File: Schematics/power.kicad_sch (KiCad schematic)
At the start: 3 parts, among them U5 AMS1117-3.3

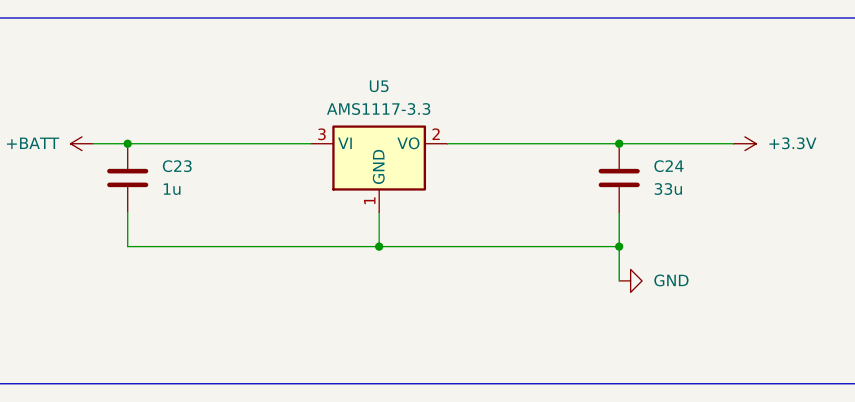
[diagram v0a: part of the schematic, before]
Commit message: added LCSC numbers and footprint values, need to connect schemeatic pins, then can start layout
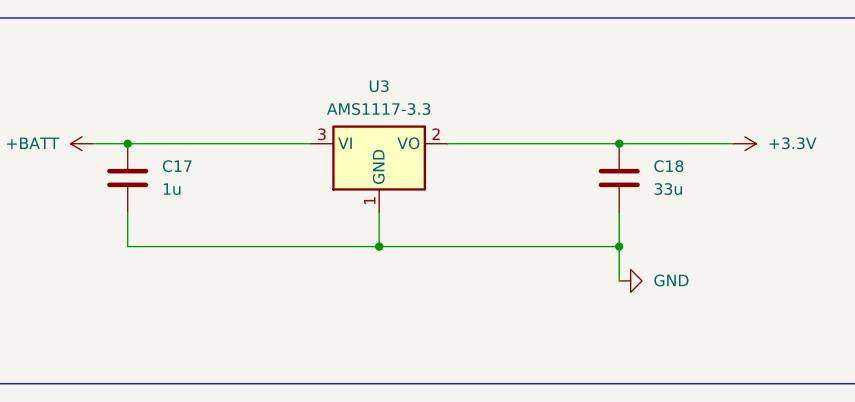
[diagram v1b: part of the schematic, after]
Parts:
- C17: renamed from C23; LCSC Part (none) -> C28323
- C18: renamed from C24; LCSC Part (none) -> C432920
- U3: renamed from U5; LCSC Part (none) -> C6186
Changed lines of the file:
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@@
 		(dnp no)
 		(fields_autoplaced yes)
-		(property "Reference" "#PWR066"
+		(property "Reference" "#PWR042"
 			(at 101.6 30.48 0)
 			(effects
@@
 			(project "flightcomputer2"
 				(path "/6cb3dda3-5fe8-4715-b831-354360aa3199/ba4deb13-717a-43bb-a60d-abfd8de92de6"
-					(reference "#PWR066")
+					(reference "#PWR042")
 					(unit 1)
 				)
@@
 		(on_board yes)
 		(dnp no)
-		(property "Reference" "C24"
+		(property "Reference" "C18"
 			(at 96.52 33.0199 0)
 			(effects
@@
 			)
 		)
+		(property "Sim.Device" ""
+			(at 92.71 34.29 0)
+			(effects
+				(font
+					(size 1.27 1.27)
+				)
+				(hide yes)
+			)
+		)
+		(property "Sim.Type" ""
+			(at 92.71 34.29 0)
+			(effects
+				(font
+					(size 1.27 1.27)
+				)
+				(hide yes)
+			)
+		)
+		(property "LCSC Part" "C432920"
+			(at 92.71 34.29 0)
+			(effects
+				(font
+					(size 1.27 1.27)
+				)
+				(hide yes)
+			)
+		)
 		(pin "2"
 		)
@@
 			(project "flightcomputer2"
 				(path "/6cb3dda3-5fe8-4715-b831-354360aa3199/ba4deb13-717a-43bb-a60d-abfd8de92de6"
-					(reference "C24")
+					(reference "C18")
 					(unit 1)
 				)
@@
 		(dnp no)
 		(fields_autoplaced yes)
-		(property "Reference" "#PWR05"
+		(property "Reference" "#PWR040"
 			(at 38.1 30.48 0)
 			(effects
@@
 			(project ""
 				(path "/6cb3dda3-5fe8-4715-b831-354360aa3199/ba4deb13-717a-43bb-a60d-abfd8de92de6"
-					(reference "#PWR05")
+					(reference "#PWR040")
 					(unit 1)
 				)
@@
 		(dnp no)
 		(fields_autoplaced yes)
-		(property "Reference" "U5"
+		(property "Reference" "U3"
 			(at 66.04 24.13 0)
 			(effects
@@
 			)
 		)
+		(property "Sim.Device" ""
+			(at 66.04 30.48 0)
+			(effects
+				(font
+					(size 1.27 1.27)
+				)
+				(hide yes)
+			)
+		)
+		(property "Sim.Type" ""
+			(at 66.04 30.48 0)
+			(effects
+				(font
+					(size 1.27 1.27)
+				)
+				(hide yes)
+			)
+		)
+		(property "LCSC Part" "C6186"
+			(at 66.04 30.48 0)
+			(effects
+				(font
+					(size 1.27 1.27)
+				)
+				(hide yes)
+			)
+		)
 		(pin "2"
 		)
@@
 			(project "flightcomputer2"
 				(path "/6cb3dda3-5fe8-4715-b831-354360aa3199/ba4deb13-717a-43bb-a60d-abfd8de92de6"
-					(reference "U5")
+					(reference "U3")
 					(unit 1)
 				)
@@
 		(dnp no)
 		(fields_autoplaced yes)
-		(property "Reference" "#PWR058"
+		(property "Reference" "#PWR041"
 			(at 99.06 45.72 0)
 			(effects
@@
 			(project "flightcomputer2"
 				(path "/6cb3dda3-5fe8-4715-b831-354360aa3199/ba4deb13-717a-43bb-a60d-abfd8de92de6"
-					(reference "#PWR058")
+					(reference "#PWR041")
 					(unit 1)
 				)
@@
 		(dnp no)
 		(fields_autoplaced yes)
-		(property "Reference" "C23"
+		(property "Reference" "C17"
 			(at 41.91 33.0199 0)
 			(effects
@@
 			)
 		)
+		(property "Sim.Device" ""
+			(at 38.1 34.29 0)
+			(effects
+				(font
+					(size 1.27 1.27)
+				)
+				(hide yes)
+			)
+		)
+		(property "Sim.Type" ""
+			(at 38.1 34.29 0)
+			(effects
+				(font
+					(size 1.27 1.27)
+				)
+				(hide yes)
+			)
+		)
+		(property "LCSC Part" "C28323"
+			(at 38.1 34.29 0)
+			(effects
+				(font
+					(size 1.27 1.27)
+				)
+				(hide yes)
+			)
+		)
 		(pin "1"
 		)
@@
 			(project "flightcomputer2"
 				(path "/6cb3dda3-5fe8-4715-b831-354360aa3199/ba4deb13-717a-43bb-a60d-abfd8de92de6"
-					(reference "C23")
-					(unit 1)
-				)
+					(reference "C17")
+					(unit 1)
+				)

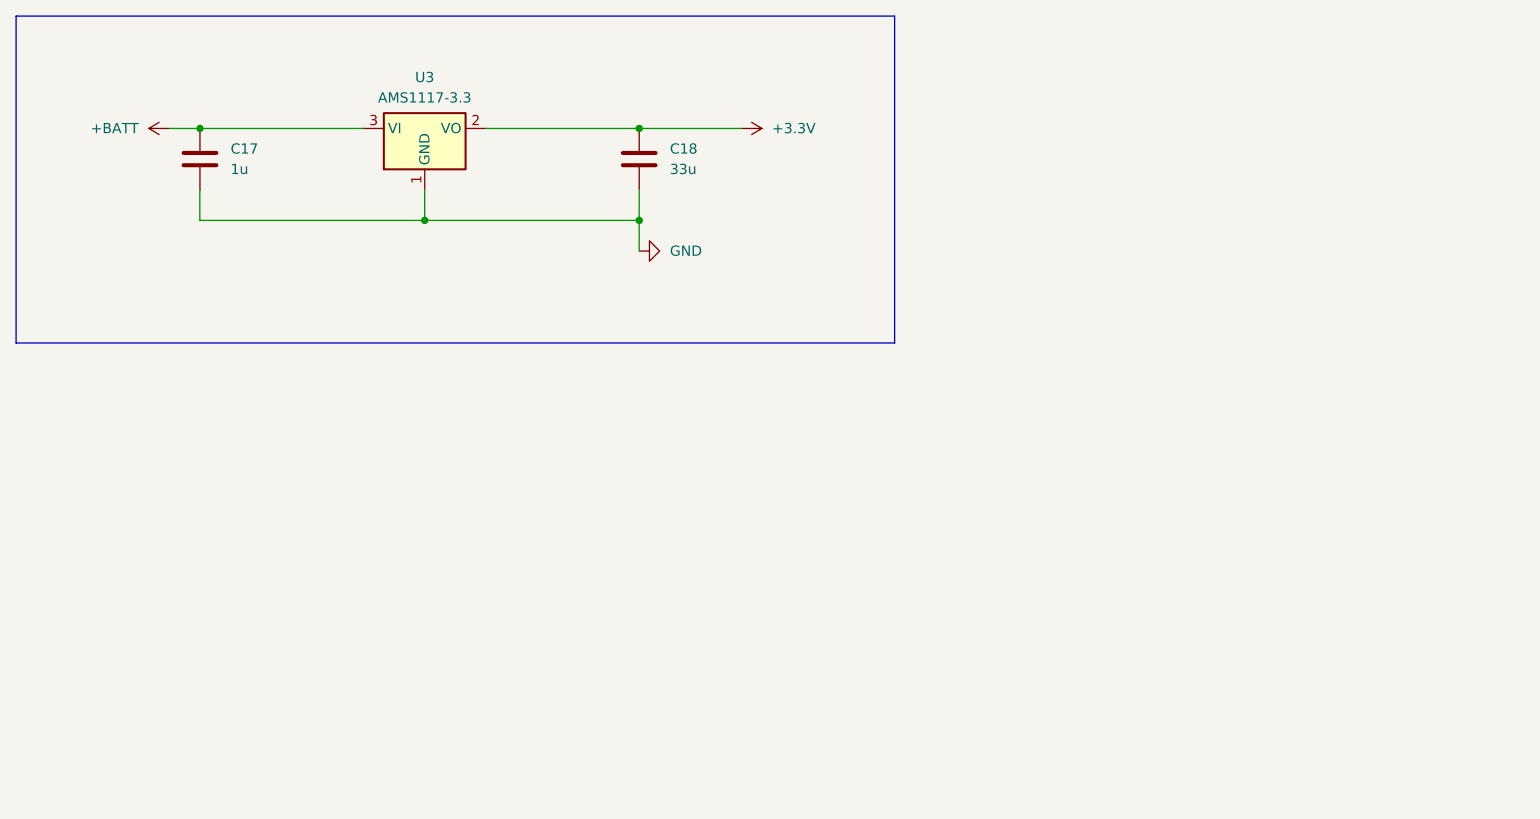
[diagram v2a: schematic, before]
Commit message: fixed symbols and added diodes to power input before ldo
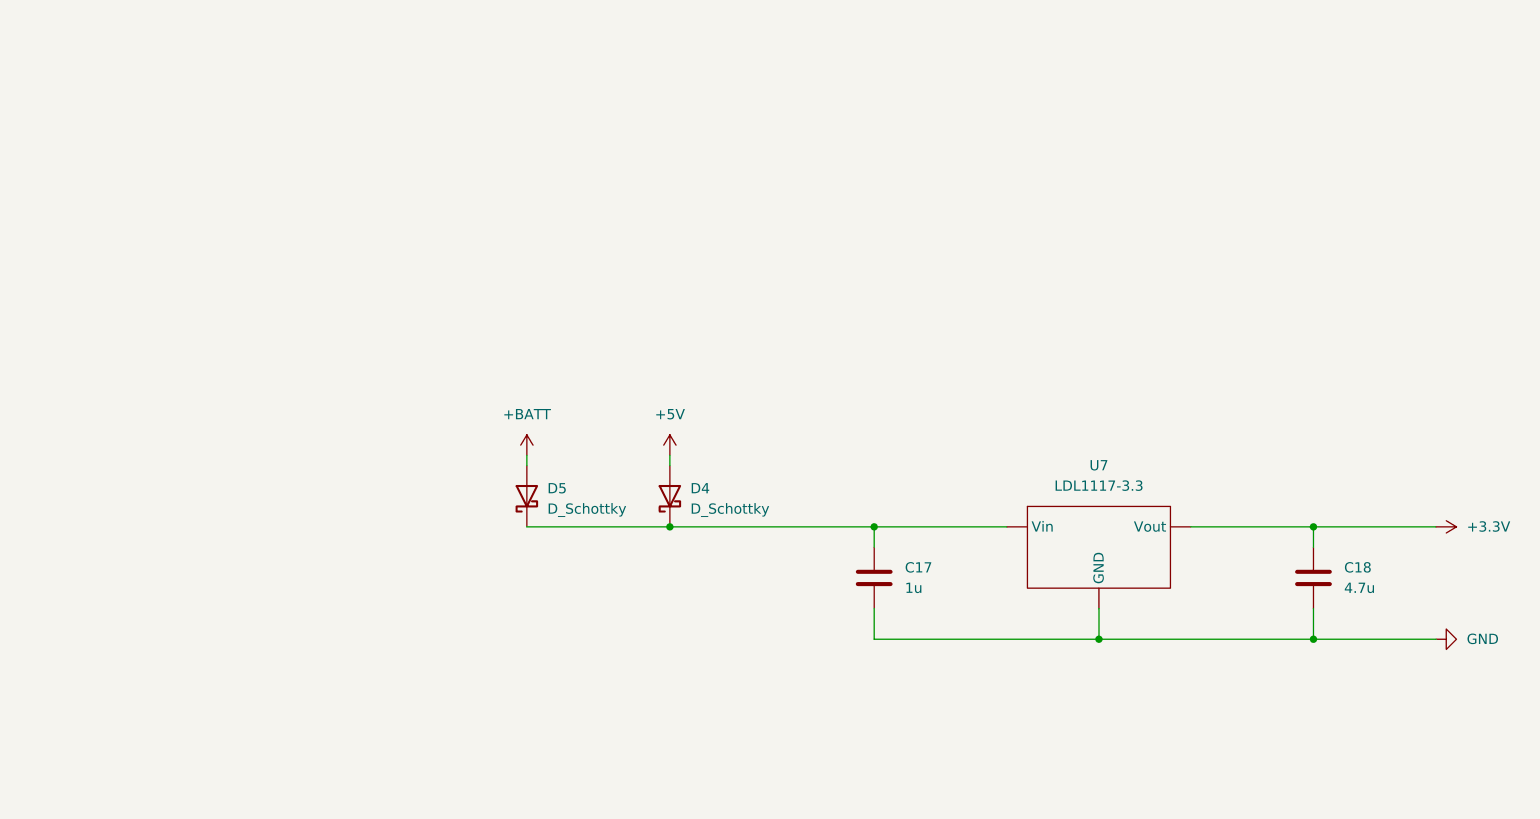
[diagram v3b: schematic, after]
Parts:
- removed U3: AMS1117-3.3, Package_TO_SOT_SMD:SOT-223-3_TabPin2, symbol Regulator_Linear:AMS1117-3.3
- added D4, D5: D_Schottky, symbol Device:D_Schottky
- added U7: LDL1117-3.3, symbol Footprints:LDL1117-3.3
- C18: value 33u -> 4.7u; LCSC Part C432920 -> C98192
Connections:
- net +3.3V: now also U7. (Vout)
- net +BATT: now also D5.2 (A); no longer C17.1
- net GND: now also U7. (Vout)
- new net: C17.1, D4.1 (K), D5.1 (K), U7. (Vout)
- new net +5V: D4.2 (A)
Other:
- moved on the sheet: C17, C18

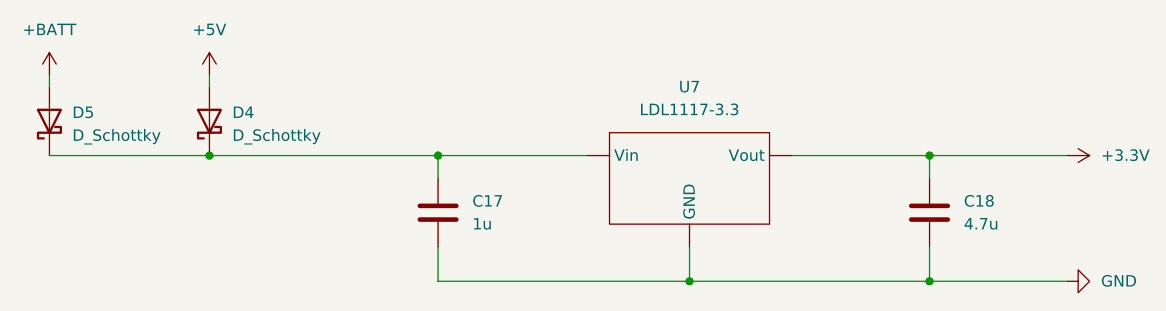
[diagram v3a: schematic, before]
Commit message: added lora correct and organizing sheet pins
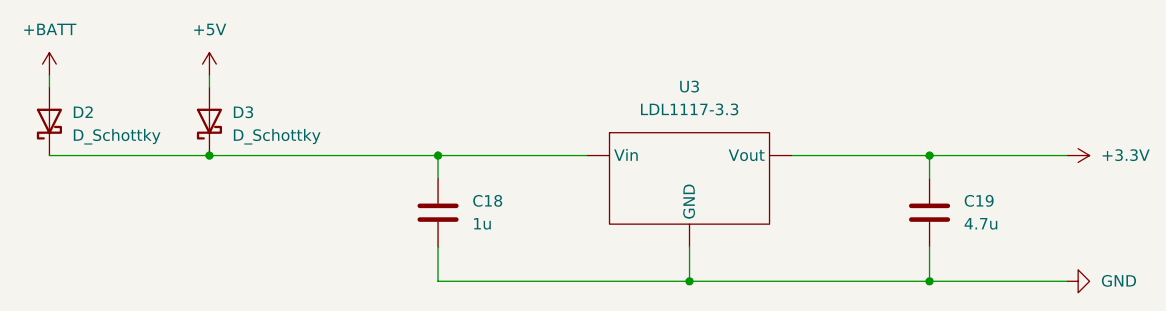
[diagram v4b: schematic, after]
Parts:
- renumbered C17 to C18, C18 to C19, D5 to D2, D4 to D3, U7 to U3
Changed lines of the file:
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@@
 		(on_board yes)
 		(dnp no)
-		(property "Reference" "D5"
+		(property "Reference" "D2"
 			(at 81.28 75.2474 90)
 			(effects
@@
 			(project "flightcomputer2"
 				(path "/6cb3dda3-5fe8-4715-b831-354360aa3199/ba4deb13-717a-43bb-a60d-abfd8de92de6"
-					(reference "D5")
+					(reference "D2")
 					(unit 1)
 				)
@@
 		(dnp no)
 		(fields_autoplaced yes)
-		(property "Reference" "D4"
+		(property "Reference" "D3"
 			(at 99.06 75.2474 90)
 			(effects
@@
 			(project ""
 				(path "/6cb3dda3-5fe8-4715-b831-354360aa3199/ba4deb13-717a-43bb-a60d-abfd8de92de6"
-					(reference "D4")
+					(reference "D3")
 					(unit 1)
 				)
@@
 		(dnp no)
 		(fields_autoplaced yes)
-		(property "Reference" "U7"
+		(property "Reference" "U3"
 			(at 149.86 72.39 0)
 			(effects
@@
 			(project ""
 				(path "/6cb3dda3-5fe8-4715-b831-354360aa3199/ba4deb13-717a-43bb-a60d-abfd8de92de6"
-					(reference "U7")
+					(reference "U3")
 					(unit 1)
 				)
@@
 		(on_board yes)
 		(dnp no)
-		(property "Reference" "C18"
+		(property "Reference" "C19"
 			(at 180.34 85.0899 0)
 			(effects
@@
 			(project "flightcomputer2"
 				(path "/6cb3dda3-5fe8-4715-b831-354360aa3199/ba4deb13-717a-43bb-a60d-abfd8de92de6"
-					(reference "C18")
+					(reference "C19")
 					(unit 1)
 				)
@@
 		(dnp no)
 		(fields_autoplaced yes)
-		(property "Reference" "#PWR041"
+		(property "Reference" "#PWR043"
 			(at 198.12 93.98 0)
 			(effects
@@
 			(project "flightcomputer2"
 				(path "/6cb3dda3-5fe8-4715-b831-354360aa3199/ba4deb13-717a-43bb-a60d-abfd8de92de6"
-					(reference "#PWR041")
+					(reference "#PWR043")
 					(unit 1)
 				)
@@
 		(dnp no)
 		(fields_autoplaced yes)
-		(property "Reference" "#PWR040"
+		(property "Reference" "#PWR041"
 			(at 96.52 74.93 0)
 			(effects
@@
 			(project ""
 				(path "/6cb3dda3-5fe8-4715-b831-354360aa3199/ba4deb13-717a-43bb-a60d-abfd8de92de6"
-					(reference "#PWR040")
+					(reference "#PWR041")
 					(unit 1)
 				)
@@
 		(dnp no)
 		(fields_autoplaced yes)
-		(property "Reference" "#PWR057"
+		(property "Reference" "#PWR040"
 			(at 78.74 74.93 0)
 			(effects
@@
 			(project "flightcomputer2"
 				(path "/6cb3dda3-5fe8-4715-b831-354360aa3199/ba4deb13-717a-43bb-a60d-abfd8de92de6"
-					(reference "#PWR057")
+					(reference "#PWR040")
 					(unit 1)
 				)
@@
 		(dnp no)
 		(fields_autoplaced yes)
-		(property "Reference" "C17"
+		(property "Reference" "C18"
 			(at 125.73 85.0899 0)
 			(effects
@@
 			(project "flightcomputer2"
 				(path "/6cb3dda3-5fe8-4715-b831-354360aa3199/ba4deb13-717a-43bb-a60d-abfd8de92de6"
-					(reference "C17")
-					(unit 1)
-				)
+					(reference "C18")
+					(unit 1)
+				)

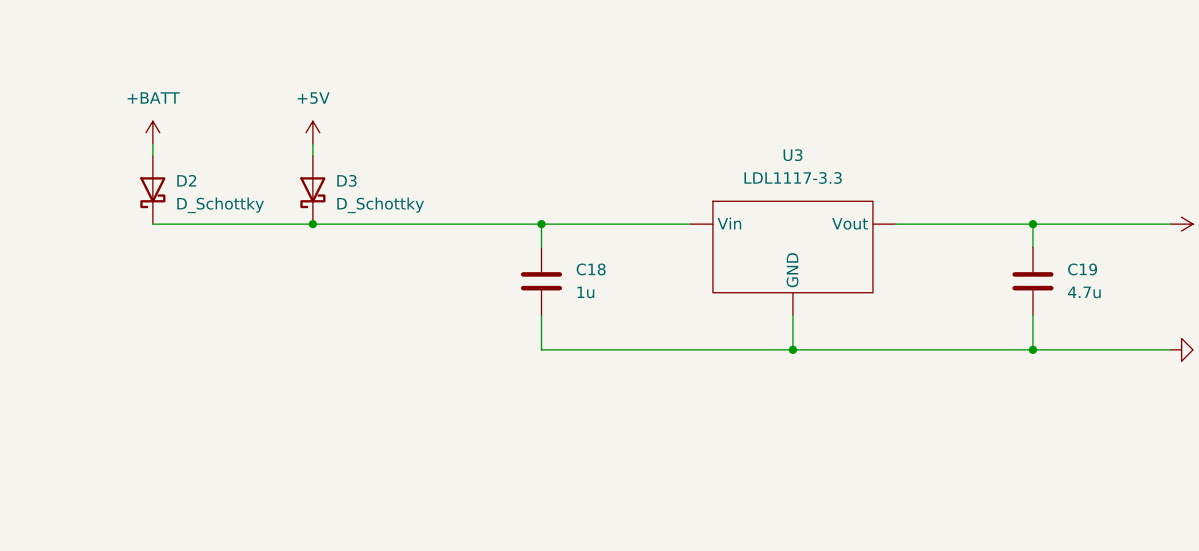
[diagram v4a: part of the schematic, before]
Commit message: finished pin assignments and ran ERC all good ready for layout
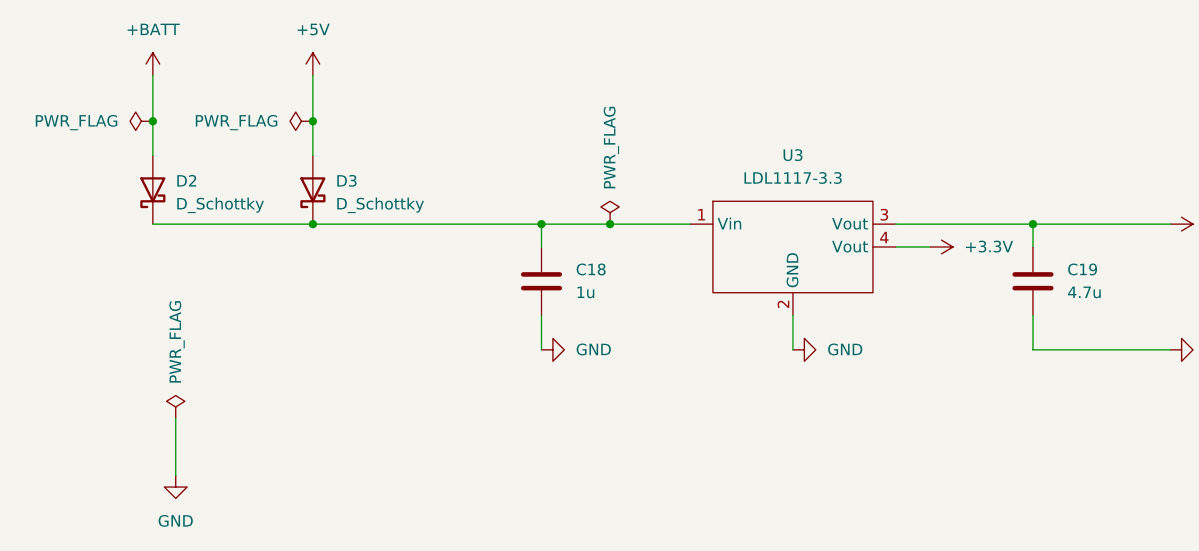
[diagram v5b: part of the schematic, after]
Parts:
- D2, D3: footprint (none) -> Diode_SMD:D_2114_3652Metric; LCSC C68883 -> (none); LCSC Part (none) -> C113936
- U3: footprint (none) -> myFootprints:SOT230P700X180-4N; LCSC C435835 -> (none); LCSC Part (none) -> C435835
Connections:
- net +3.3V: now also U3.3 (Vout), U3.4 (Vout); no longer U3. (Vout)
- net GND: now also U3.2 (GND); no longer U3. (Vout)
- net at C18.1, D2.1 (K), D3.1 (K): now also U3.1 (Vin); no longer U3. (Vout)

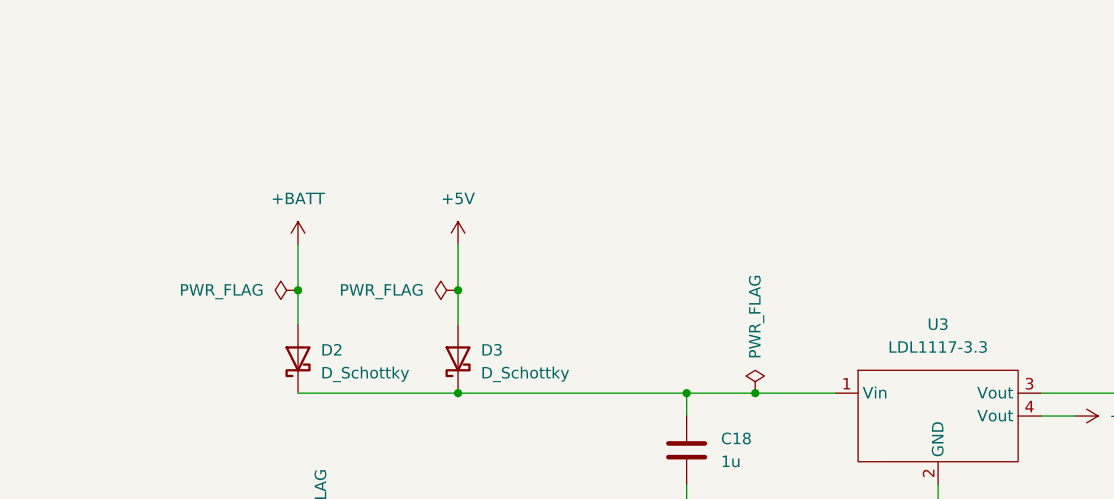
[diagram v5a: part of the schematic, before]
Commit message: first layout need to go over schematic
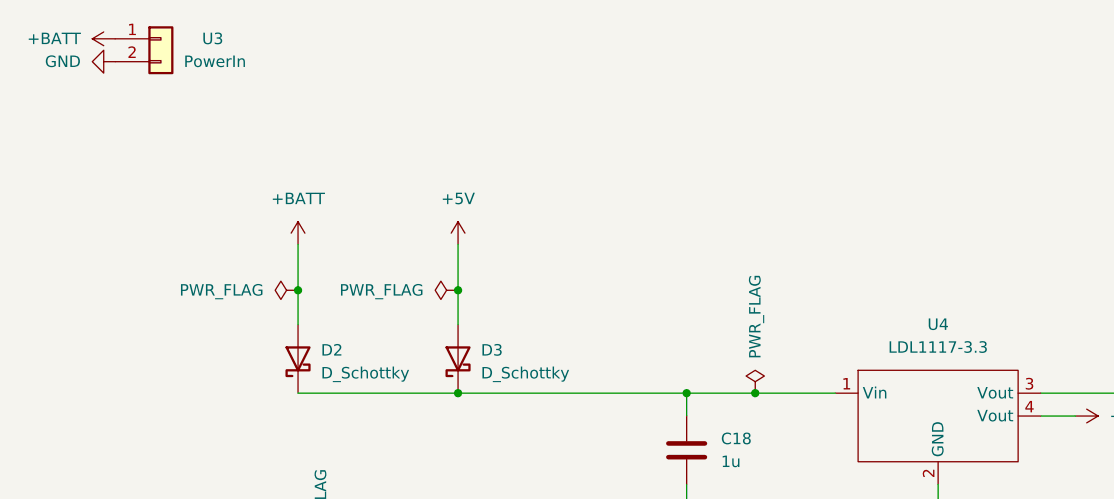
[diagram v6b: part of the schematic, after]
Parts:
- added U3: PowerIn, myFootprints:MOLEX_26013114, symbol Connector_Generic:Conn_01x02
- renumbered U3 to U4
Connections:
- net +BATT: now also U3.1 (Pin_1)
- net GND: now also U3.2 (Pin_2)
